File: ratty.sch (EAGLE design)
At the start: 94 parts, among them IC2 L293DD, Q1 BS170, Q2 BS170, Q3 BS170, Q5 BS170, U1 ITG-32001:1

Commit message: fixed more MCU
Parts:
- added C33: 1uF, rcl:C-EUC0603
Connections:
- net 3.3V: now also C33.1
- net AGND: now also C33.2
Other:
- moved on the sheet: C10
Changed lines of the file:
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@@
 <part name="C32" library="rcl" deviceset="C-EU" device="C0603" value="4.7uF"/>
 <part name="GND35" library="SparkFun-Aesthetics" deviceset="DGND" device=""/>
+<part name="C33" library="rcl" deviceset="C-EU" device="C0603" value="1uF"/>
 </parts>
 <sheets>
@@
 <instance part="IC2" gate="G$1" x="233.68" y="35.56"/>
 <instance part="U$4" gate="G$1" x="132.08" y="276.86"/>
-<instance part="C10" gate="G$1" x="-93.98" y="228.6"/>
+<instance part="C10" gate="G$1" x="-101.6" y="228.6"/>
 <instance part="C11" gate="G$1" x="-73.66" y="200.66"/>
 <instance part="C16" gate="G$1" x="-53.34" y="200.66"/>
@@
 <instance part="C32" gate="G$1" x="33.02" y="200.66"/>
 <instance part="GND35" gate="G$1" x="33.02" y="185.42"/>
+<instance part="C33" gate="G$1" x="-88.9" y="228.6"/>
 </instances>
 <busses>
@@
 </segment>
 <segment>
-<pinref part="C10" gate="G$1" pin="1"/>
-<wire x1="-93.98" y1="231.14" x2="-93.98" y2="233.68" width="0.1524" layer="91"/>
 <label x="-93.98" y="238.76" size="1.778" layer="95" rot="R90" xref="yes"/>
 <pinref part="U$22" gate="G$1" pin="2"/>
 <wire x1="-93.98" y1="233.68" x2="-93.98" y2="238.76" width="0.1524" layer="91"/>
+<pinref part="C10" gate="G$1" pin="1"/>
+<wire x1="-101.6" y1="231.14" x2="-93.98" y2="231.14" width="0.1524" layer="91"/>
+<wire x1="-93.98" y1="231.14" x2="-93.98" y2="233.68" width="0.1524" layer="91"/>
 <junction x="-93.98" y="233.68"/>
+<pinref part="C33" gate="G$1" pin="1"/>
+<wire x1="-93.98" y1="231.14" x2="-88.9" y2="231.14" width="0.1524" layer="91"/>
+<junction x="-93.98" y="231.14"/>
 </segment>
 <segment>
@@
 </segment>
 <segment>
-<pinref part="C10" gate="G$1" pin="2"/>
-<wire x1="-93.98" y1="223.52" x2="-93.98" y2="220.98" width="0.1524" layer="91"/>
 <pinref part="U$7" gate="G$1" pin="2"/>
 <wire x1="-93.98" y1="220.98" x2="-93.98" y2="215.9" width="0.1524" layer="91"/>
+<pinref part="AGND9" gate="VR1" pin="AGND"/>
+<pinref part="C10" gate="G$1" pin="2"/>
+<wire x1="-101.6" y1="223.52" x2="-93.98" y2="223.52" width="0.1524" layer="91"/>
+<wire x1="-93.98" y1="223.52" x2="-93.98" y2="220.98" width="0.1524" layer="91"/>
 <junction x="-93.98" y="220.98"/>
-<pinref part="AGND9" gate="VR1" pin="AGND"/>
-</segment>
-</net>
+<pinref part="C33" gate="G$1" pin="2"/>
+<wire x1="-93.98" y1="223.52" x2="-88.9" y2="223.52" width="0.1524" layer="91"/>
+<junction x="-93.98" y="223.52"/>
+</segment>
+</net>

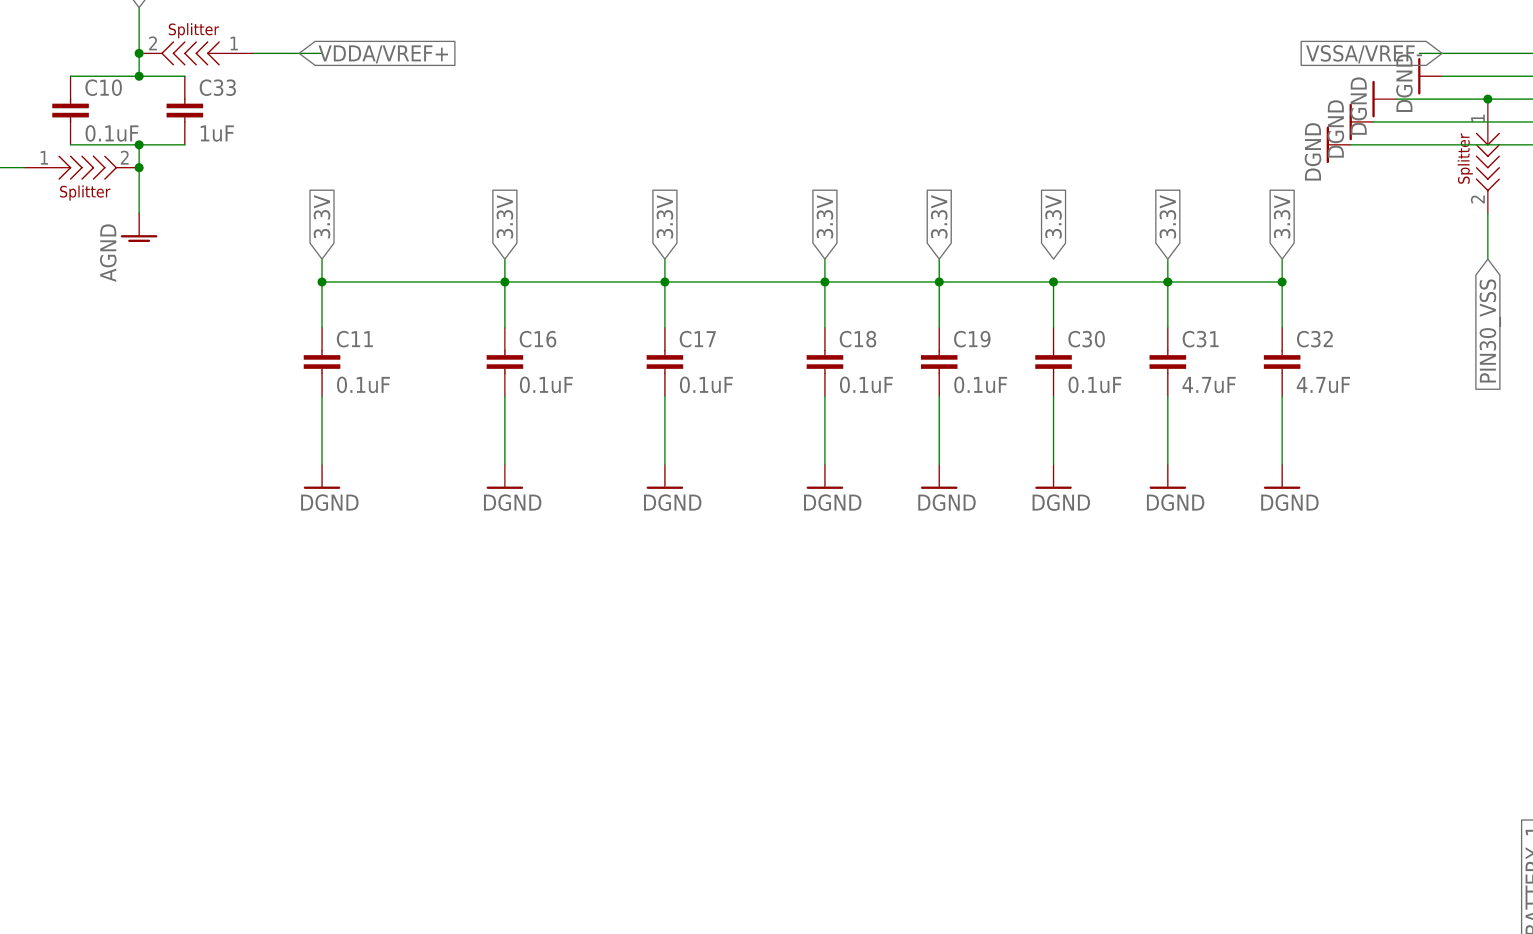
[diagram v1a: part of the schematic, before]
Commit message: Made board larger to incorporate switch
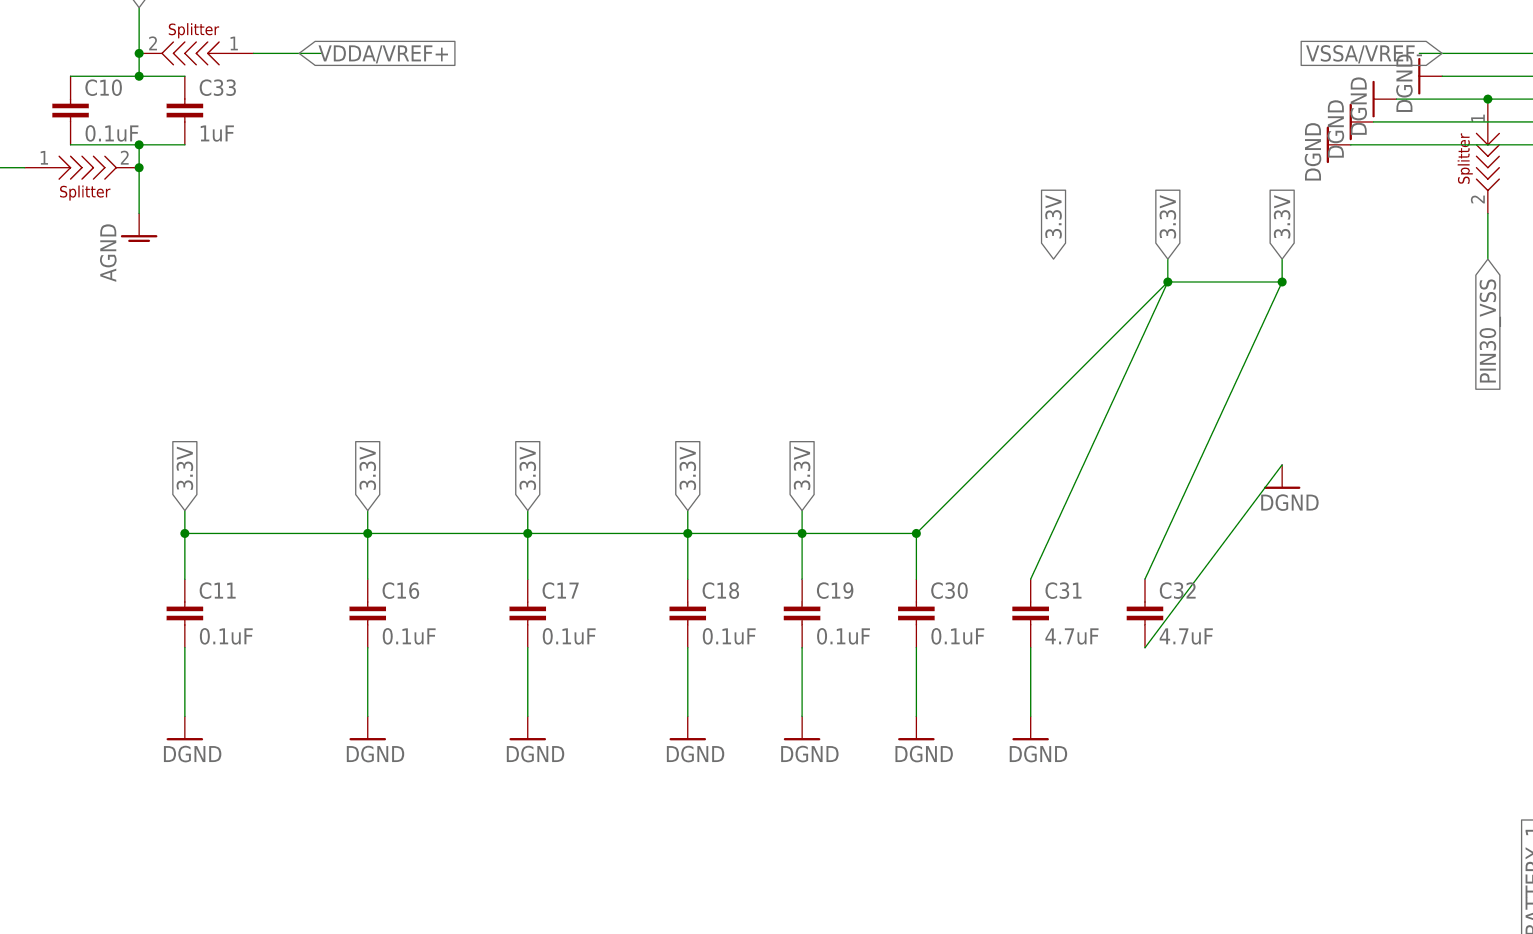
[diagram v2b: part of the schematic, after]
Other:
- moved on the sheet: C11, C16, C17, C18, C19, C30, C31, C32
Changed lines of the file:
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@@
 <instance part="U$4" gate="G$1" x="132.08" y="276.86"/>
 <instance part="C10" gate="G$1" x="-101.6" y="228.6"/>
-<instance part="C11" gate="G$1" x="-73.66" y="200.66"/>
-<instance part="C16" gate="G$1" x="-53.34" y="200.66"/>
-<instance part="C17" gate="G$1" x="-35.56" y="200.66"/>
-<instance part="C18" gate="G$1" x="-17.78" y="200.66"/>
-<instance part="C19" gate="G$1" x="-5.08" y="200.66"/>
+<instance part="C11" gate="G$1" x="-88.9" y="172.72"/>
+<instance part="C16" gate="G$1" x="-68.58" y="172.72"/>
+<instance part="C17" gate="G$1" x="-50.8" y="172.72"/>
+<instance part="C18" gate="G$1" x="-33.02" y="172.72"/>
+<instance part="C19" gate="G$1" x="-20.32" y="172.72"/>
 <instance part="R2" gate="G$1" x="5.08" y="294.64"/>
 <instance part="RESETBUTTON" gate="G$1" x="-20.32" y="281.94" rot="R180"/>
@@
 <instance part="U$22" gate="G$1" x="-88.9" y="233.68" rot="R180"/>
 <instance part="AGND9" gate="VR1" x="-93.98" y="213.36"/>
-<instance part="GND28" gate="G$1" x="-73.66" y="185.42"/>
-<instance part="GND29" gate="G$1" x="-53.34" y="185.42"/>
-<instance part="GND30" gate="G$1" x="-35.56" y="185.42"/>
-<instance part="GND31" gate="G$1" x="-17.78" y="185.42"/>
-<instance part="C30" gate="G$1" x="7.62" y="200.66"/>
-<instance part="GND32" gate="G$1" x="-5.08" y="185.42"/>
-<instance part="GND33" gate="G$1" x="7.62" y="185.42"/>
-<instance part="C31" gate="G$1" x="20.32" y="200.66"/>
-<instance part="GND34" gate="G$1" x="20.32" y="185.42"/>
-<instance part="C32" gate="G$1" x="33.02" y="200.66"/>
+<instance part="GND28" gate="G$1" x="-88.9" y="157.48"/>
+<instance part="GND29" gate="G$1" x="-68.58" y="157.48"/>
+<instance part="GND30" gate="G$1" x="-50.8" y="157.48"/>
+<instance part="GND31" gate="G$1" x="-33.02" y="157.48"/>
+<instance part="C30" gate="G$1" x="-7.62" y="172.72"/>
+<instance part="GND32" gate="G$1" x="-20.32" y="157.48"/>
+<instance part="GND33" gate="G$1" x="-7.62" y="157.48"/>
+<instance part="C31" gate="G$1" x="5.08" y="172.72"/>
+<instance part="GND34" gate="G$1" x="5.08" y="157.48"/>
+<instance part="C32" gate="G$1" x="17.78" y="172.72"/>
 <instance part="GND35" gate="G$1" x="33.02" y="185.42"/>
 <instance part="C33" gate="G$1" x="-88.9" y="228.6"/>
@@
 <segment>
 <pinref part="C11" gate="G$1" pin="1"/>
-<wire x1="-73.66" y1="210.82" x2="-73.66" y2="208.28" width="0.1524" layer="91"/>
-<wire x1="-73.66" y1="208.28" x2="-73.66" y2="203.2" width="0.1524" layer="91"/>
-<label x="-73.66" y="210.82" size="1.778" layer="95" rot="R90" xref="yes"/>
+<wire x1="-88.9" y1="182.88" x2="-88.9" y2="180.34" width="0.1524" layer="91"/>
+<wire x1="-88.9" y1="180.34" x2="-88.9" y2="175.26" width="0.1524" layer="91"/>
+<label x="-88.9" y="182.88" size="1.778" layer="95" rot="R90" xref="yes"/>
 <pinref part="C16" gate="G$1" pin="1"/>
-<wire x1="-53.34" y1="210.82" x2="-53.34" y2="208.28" width="0.1524" layer="91"/>
-<wire x1="-53.34" y1="208.28" x2="-53.34" y2="203.2" width="0.1524" layer="91"/>
-<wire x1="-73.66" y1="208.28" x2="-53.34" y2="208.28" width="0.1524" layer="91"/>
-<junction x="-73.66" y="208.28"/>
-<junction x="-53.34" y="208.28"/>
+<wire x1="-68.58" y1="182.88" x2="-68.58" y2="180.34" width="0.1524" layer="91"/>
+<wire x1="-68.58" y1="180.34" x2="-68.58" y2="175.26" width="0.1524" layer="91"/>
+<wire x1="-88.9" y1="180.34" x2="-68.58" y2="180.34" width="0.1524" layer="91"/>
+<junction x="-88.9" y="180.34"/>
+<junction x="-68.58" y="180.34"/>
 <pinref part="C17" gate="G$1" pin="1"/>
-<wire x1="-35.56" y1="210.82" x2="-35.56" y2="208.28" width="0.1524" layer="91"/>
-<wire x1="-35.56" y1="208.28" x2="-35.56" y2="203.2" width="0.1524" layer="91"/>
-<wire x1="-53.34" y1="208.28" x2="-35.56" y2="208.28" width="0.1524" layer="91"/>
-<junction x="-35.56" y="208.28"/>
+<wire x1="-50.8" y1="182.88" x2="-50.8" y2="180.34" width="0.1524" layer="91"/>
+<wire x1="-50.8" y1="180.34" x2="-50.8" y2="175.26" width="0.1524" layer="91"/>
+<wire x1="-68.58" y1="180.34" x2="-50.8" y2="180.34" width="0.1524" layer="91"/>
+<junction x="-50.8" y="180.34"/>
 <pinref part="C18" gate="G$1" pin="1"/>
-<wire x1="-17.78" y1="210.82" x2="-17.78" y2="208.28" width="0.1524" layer="91"/>
-<wire x1="-17.78" y1="208.28" x2="-17.78" y2="203.2" width="0.1524" layer="91"/>
-<wire x1="-35.56" y1="208.28" x2="-17.78" y2="208.28" width="0.1524" layer="91"/>
-<junction x="-17.78" y="208.28"/>
+<wire x1="-33.02" y1="182.88" x2="-33.02" y2="180.34" width="0.1524" layer="91"/>
+<wire x1="-33.02" y1="180.34" x2="-33.02" y2="175.26" width="0.1524" layer="91"/>
+<wire x1="-50.8" y1="180.34" x2="-33.02" y2="180.34" width="0.1524" layer="91"/>
+<junction x="-33.02" y="180.34"/>
 <pinref part="C19" gate="G$1" pin="1"/>
-<wire x1="-5.08" y1="210.82" x2="-5.08" y2="208.28" width="0.1524" layer="91"/>
-<wire x1="-5.08" y1="208.28" x2="-5.08" y2="203.2" width="0.1524" layer="91"/>
-<wire x1="-17.78" y1="208.28" x2="-5.08" y2="208.28" width="0.1524" layer="91"/>
-<junction x="-5.08" y="208.28"/>
+<wire x1="-20.32" y1="182.88" x2="-20.32" y2="180.34" width="0.1524" layer="91"/>
+<wire x1="-20.32" y1="180.34" x2="-20.32" y2="175.26" width="0.1524" layer="91"/>
+<wire x1="-33.02" y1="180.34" x2="-20.32" y2="180.34" width="0.1524" layer="91"/>
+<junction x="-20.32" y="180.34"/>
 <pinref part="C30" gate="G$1" pin="1"/>
-<wire x1="7.62" y1="203.2" x2="7.62" y2="208.28" width="0.1524" layer="91"/>
-<wire x1="7.62" y1="208.28" x2="-5.08" y2="208.28" width="0.1524" layer="91"/>
+<wire x1="-7.62" y1="175.26" x2="-7.62" y2="180.34" width="0.1524" layer="91"/>
+<wire x1="-7.62" y1="180.34" x2="-20.32" y2="180.34" width="0.1524" layer="91"/>
 <pinref part="C31" gate="G$1" pin="1"/>
-<wire x1="7.62" y1="208.28" x2="20.32" y2="208.28" width="0.1524" layer="91"/>
-<wire x1="20.32" y1="208.28" x2="20.32" y2="203.2" width="0.1524" layer="91"/>
-<junction x="7.62" y="208.28"/>
-<label x="-53.34" y="210.82" size="1.778" layer="95" rot="R90" xref="yes"/>
-<label x="-35.56" y="210.82" size="1.778" layer="95" rot="R90" xref="yes"/>
-<label x="-17.78" y="210.82" size="1.778" layer="95" rot="R90" xref="yes"/>
-<label x="-5.08" y="210.82" size="1.778" layer="95" rot="R90" xref="yes"/>
+<wire x1="-7.62" y1="180.34" x2="20.32" y2="208.28" width="0.1524" layer="91"/>
+<wire x1="20.32" y1="208.28" x2="5.08" y2="175.26" width="0.1524" layer="91"/>
+<junction x="-7.62" y="180.34"/>
+<label x="-68.58" y="182.88" size="1.778" layer="95" rot="R90" xref="yes"/>
+<label x="-50.8" y="182.88" size="1.778" layer="95" rot="R90" xref="yes"/>
+<label x="-33.02" y="182.88" size="1.778" layer="95" rot="R90" xref="yes"/>
+<label x="-20.32" y="182.88" size="1.778" layer="95" rot="R90" xref="yes"/>
 <label x="7.62" y="210.82" size="1.778" layer="95" rot="R90" xref="yes"/>
 <label x="20.32" y="210.82" size="1.778" layer="95" rot="R90" xref="yes"/>
 <pinref part="C32" gate="G$1" pin="1"/>
 <wire x1="20.32" y1="208.28" x2="33.02" y2="208.28" width="0.1524" layer="91"/>
-<wire x1="33.02" y1="208.28" x2="33.02" y2="203.2" width="0.1524" layer="91"/>
+<wire x1="33.02" y1="208.28" x2="17.78" y2="175.26" width="0.1524" layer="91"/>
 <junction x="20.32" y="208.28"/>
 <wire x1="20.32" y1="208.28" x2="20.32" y2="210.82" width="0.1524" layer="91"/>
@@
 <segment>
 <pinref part="C11" gate="G$1" pin="2"/>
-<wire x1="-73.66" y1="195.58" x2="-73.66" y2="187.96" width="0.1524" layer="91"/>
+<wire x1="-88.9" y1="167.64" x2="-88.9" y2="160.02" width="0.1524" layer="91"/>
 <pinref part="GND28" gate="G$1" pin="GND"/>
 </segment>
 <segment>
 <pinref part="C16" gate="G$1" pin="2"/>
-<wire x1="-53.34" y1="195.58" x2="-53.34" y2="187.96" width="0.1524" layer="91"/>
+<wire x1="-68.58" y1="167.64" x2="-68.58" y2="160.02" width="0.1524" layer="91"/>
 <pinref part="GND29" gate="G$1" pin="GND"/>
 </segment>
@@
 <pinref part="C17" gate="G$1" pin="2"/>
 <pinref part="GND30" gate="G$1" pin="GND"/>
-<wire x1="-35.56" y1="195.58" x2="-35.56" y2="187.96" width="0.1524" layer="91"/>
+<wire x1="-50.8" y1="167.64" x2="-50.8" y2="160.02" width="0.1524" layer="91"/>
 </segment>
 <segment>
 <pinref part="C18" gate="G$1" pin="2"/>
 <pinref part="GND31" gate="G$1" pin="GND"/>
-<wire x1="-17.78" y1="195.58" x2="-17.78" y2="187.96" width="0.1524" layer="91"/>
+<wire x1="-33.02" y1="167.64" x2="-33.02" y2="160.02" width="0.1524" layer="91"/>
 </segment>
 <segment>
 <pinref part="C19" gate="G$1" pin="2"/>
-<wire x1="-5.08" y1="195.58" x2="-5.08" y2="187.96" width="0.1524" layer="91"/>
+<wire x1="-20.32" y1="167.64" x2="-20.32" y2="160.02" width="0.1524" layer="91"/>
 <pinref part="GND32" gate="G$1" pin="GND"/>
 </segment>
 <segment>
 <pinref part="C30" gate="G$1" pin="2"/>
-<wire x1="7.62" y1="195.58" x2="7.62" y2="187.96" width="0.1524" layer="91"/>
+<wire x1="-7.62" y1="167.64" x2="-7.62" y2="160.02" width="0.1524" layer="91"/>
 <pinref part="GND33" gate="G$1" pin="GND"/>
 </segment>
 <segment>
 <pinref part="C31" gate="G$1" pin="2"/>
-<wire x1="20.32" y1="195.58" x2="20.32" y2="187.96" width="0.1524" layer="91"/>
+<wire x1="5.08" y1="167.64" x2="5.08" y2="160.02" width="0.1524" layer="91"/>
 <pinref part="GND34" gate="G$1" pin="GND"/>
 </segment>
 <segment>
 <pinref part="C32" gate="G$1" pin="2"/>
-<wire x1="33.02" y1="195.58" x2="33.02" y2="187.96" width="0.1524" layer="91"/>
+<wire x1="17.78" y1="167.64" x2="33.02" y2="187.96" width="0.1524" layer="91"/>
 <pinref part="GND35" gate="G$1" pin="GND"/>
 </segment>

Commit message: routing
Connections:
- removed net PV6_TX_PIN: JP1.4
- net PC6_TX_PIN: now also JP1.4
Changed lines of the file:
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@@
 <?xml version="1.0" encoding="utf-8"?>
 <!DOCTYPE eagle SYSTEM "eagle.dtd">
-<eagle version="7.5.0">
+<eagle version="7.7.0">
 <drawing>
 <settings>
@@
 <instance part="GND34" gate="G$1" x="5.08" y="157.48"/>
 <instance part="C32" gate="G$1" x="17.78" y="172.72"/>
-<instance part="GND35" gate="G$1" x="33.02" y="185.42"/>
+<instance part="GND35" gate="G$1" x="17.78" y="157.48"/>
 <instance part="C33" gate="G$1" x="-88.9" y="228.6"/>
 </instances>
@@
 <wire x1="-7.62" y1="180.34" x2="-20.32" y2="180.34" width="0.1524" layer="91"/>
 <pinref part="C31" gate="G$1" pin="1"/>
-<wire x1="-7.62" y1="180.34" x2="20.32" y2="208.28" width="0.1524" layer="91"/>
-<wire x1="20.32" y1="208.28" x2="5.08" y2="175.26" width="0.1524" layer="91"/>
+<wire x1="-7.62" y1="180.34" x2="5.08" y2="180.34" width="0.1524" layer="91"/>
+<wire x1="5.08" y1="180.34" x2="5.08" y2="175.26" width="0.1524" layer="91"/>
 <junction x="-7.62" y="180.34"/>
 <label x="-68.58" y="182.88" size="1.778" layer="95" rot="R90" xref="yes"/>
@@
 <label x="-33.02" y="182.88" size="1.778" layer="95" rot="R90" xref="yes"/>
 <label x="-20.32" y="182.88" size="1.778" layer="95" rot="R90" xref="yes"/>
-<label x="7.62" y="210.82" size="1.778" layer="95" rot="R90" xref="yes"/>
-<label x="20.32" y="210.82" size="1.778" layer="95" rot="R90" xref="yes"/>
+<label x="-7.62" y="180.34" size="1.778" layer="95" rot="R90" xref="yes"/>
+<label x="5.08" y="182.88" size="1.778" layer="95" rot="R90" xref="yes"/>
 <pinref part="C32" gate="G$1" pin="1"/>
-<wire x1="20.32" y1="208.28" x2="33.02" y2="208.28" width="0.1524" layer="91"/>
-<wire x1="33.02" y1="208.28" x2="17.78" y2="175.26" width="0.1524" layer="91"/>
-<junction x="20.32" y="208.28"/>
-<wire x1="20.32" y1="208.28" x2="20.32" y2="210.82" width="0.1524" layer="91"/>
-<wire x1="33.02" y1="208.28" x2="33.02" y2="210.82" width="0.1524" layer="91"/>
-<junction x="33.02" y="208.28"/>
-<label x="33.02" y="210.82" size="1.778" layer="95" rot="R90" xref="yes"/>
+<wire x1="5.08" y1="180.34" x2="17.78" y2="180.34" width="0.1524" layer="91"/>
+<wire x1="17.78" y1="180.34" x2="17.78" y2="175.26" width="0.1524" layer="91"/>
+<junction x="5.08" y="180.34"/>
+<wire x1="5.08" y1="180.34" x2="5.08" y2="182.88" width="0.1524" layer="91"/>
+<wire x1="17.78" y1="180.34" x2="17.78" y2="182.88" width="0.1524" layer="91"/>
+<junction x="17.78" y="180.34"/>
+<label x="17.78" y="182.88" size="1.778" layer="95" rot="R90" xref="yes"/>
 </segment>
 <segment>
@@
 <segment>
 <pinref part="C32" gate="G$1" pin="2"/>
-<wire x1="17.78" y1="167.64" x2="33.02" y2="187.96" width="0.1524" layer="91"/>
 <pinref part="GND35" gate="G$1" pin="GND"/>
+<wire x1="17.78" y1="160.02" x2="17.78" y2="167.64" width="0.1524" layer="91"/>
 </segment>
 </net>
@@
 <label x="50.8" y="256.54" size="1.778" layer="95" rot="R180" xref="yes"/>
 </segment>
-</net>
-<net name="PV6_TX_PIN" class="0">
 <segment>
 <pinref part="JP1" gate="A" pin="4"/>

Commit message: Fixed errors in schematics
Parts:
- removed SPLIT_GYRO_LOGIC, SPLIT_GYRO_VDD, SPLIT_VSS_CAP, U$22, U$7: SPLITTER, splitter:SPLITTER
- JP1: value (none) -> ConnectorPins
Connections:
- removed net GRYOREGOUT: U1.REGOUT
- removed net GRYOVLOGIC: U1.VLOGIC
- removed net GYROVDD: C22.1, SPLIT_GYRO_VDD.1, U1.VDD
- removed net PA4_GYROLOGIC: SPLIT_GYRO_LOGIC.2, U$4.PA4-SPI1_NSS/I2S1_WS/SPI3_NSS/USART2_CK
- removed net PIN30_VSS: C26.2, SPLIT_VSS_CAP.2
- removed net VDDA/VREF+: U$22.1
- removed net VSSA/VREF-: U$7.1
- net 3.3V: now also C22.1, U$17.A, U$4.VDD@1, U$4.VDD@2, U$4.VDD@3, U$4.VDD@4, U$4.VDDA/VREF+, U1.VDD; no longer U$22.2
- net 5V: no longer SPLIT_GYRO_VDD.2
- net AGND: now also U$4.VSSA/VREF-, U1.AD0, U1.GND, U1.INT, U1.RESV-G; no longer U$7.2
- net DGND: now also C26.2, D_SPLITTER.2, U$4.BOOT0, U$4.VSS@1, U$4.VSS@2, U$4.VSS@3, U$4.VSS@4; no longer SPLIT_VSS_CAP.1, U$17.A, U1.GND, U1.RESV-G
- net GND: no longer D_SPLITTER.2, U1.AD0, U1.INT
- net GYROREGOUT: now also U1.REGOUT
- net GYROVLOGIC: now also U$4.PA4-SPI1_NSS/I2S1_WS/SPI3_NSS/USART2_CK, U1.VLOGIC; no longer SPLIT_GYRO_LOGIC.1
- net PA_0_ENCODER1_1: now also U$4.PA0-TIM2_CH1/TIM2_ET/TIM5_CH1
- net PA_1_ENCODER1_2: now also U$4.PA1-TIM2_CH2/TIM5_CH2/SPI4_MOSI/I2S4_SD
- net PA_6_REC_CIRCUIT_2: now also U$4.PA6-TIM1_BKIN/TIM3_CH1/SPI1_MISO/SDIO_CMD
- net PB_0_EMIT_CIRCUIT_3: now also U$4.PB0-TIM1_CH2N/TIM3_CH3/SPI5_SCK
- net PC_10_EMIT_CIRCUIT_1: now also U$4.PC10-SPI3_SCK/I2S3_CK/SDIO_D2
- net PC_11_EMIT_CIRCUIT_2: now also U$4.PC11-I2S3EXT_SD/SPI3_MISO/SDIO_D3
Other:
- moved on the sheet: C20, C22, U$4
